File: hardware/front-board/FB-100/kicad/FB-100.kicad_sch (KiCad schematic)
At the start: 0 parts

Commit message: Close LB FB schematic freeze
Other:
- note added: "Reviewed FB-100 value-bearing schematic inputs: - JFB1 24-pin interface with USB_D_P, USB_D_N, USB_CC1, USB_CC2, USB_VBUS_SENSE, FB_3V3_IO, GND, status RGB, CH_LED_1..CH_LED_10, SERVICE_BTN, RESET_BTN, OLED_SCL, OLED_SDA. - USB-C service is device-only; CC Rd behavior; ESD protection; VBUS sense-only; no back-power into LB-100 or PB-100. - UI hardware stays role-free: channel/status indicators on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"
- note added: "Schematic freeze evidence: - ../FB-100-schematic-review-closeout.md - ../FB-100-interface-signal-plan.csv - ../FB-100-interface-pinout-closeout.csv - ../FB-100-usb-service-closeout-precheck.csv - ../FB-100-ui-control-closeout-precheck.csv - ../FB-100-ui-mechanical-precheck.csv - ../FB-100-mechanical-envelope-precheck.csv - ../FB-100-component-sourcing-precheck.csv PCB layout and manufacturing out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"
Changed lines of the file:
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@@
+    )
+  )
+  (text "Reviewed FB-100 value-bearing schematic inputs:\n- JFB1 24-pin interface with USB_D_P, USB_D_N, USB_CC1, USB_CC2, USB_VBUS_SENSE, FB_3V3_IO, GND, status RGB, CH_LED_1..CH_LED_10, SERVICE_BTN, RESET_BTN, OLED_SCL, OLED_SDA.\n- USB-C service is device-only; CC Rd behavior; ESD protection; VBUS sense-only; no back-power into LB-100 or PB-100.\n- UI hardware stays role-free: channel/status indicators only, no accessory names.\n- Optional OLED remains DNP until mechanical and power review.\n- Mechanical envelope, USB access, LED/button alignment, service sealing, and enclosure boundary are reviewed."
+    (at 130 30 0)
+    (effects
+      (font
+        (size 1.45 1.45)
+      )
+      (justify left top)
+    )
+  )
+  (text "Schematic freeze evidence:\n- ../FB-100-schematic-review-closeout.md\n- ../FB-100-interface-signal-plan.csv\n- ../FB-100-interface-pinout-closeout.csv\n- ../FB-100-usb-service-closeout-precheck.csv\n- ../FB-100-ui-control-closeout-precheck.csv\n- ../FB-100-ui-mechanical-precheck.csv\n- ../FB-100-mechanical-envelope-precheck.csv\n- ../FB-100-component-sourcing-precheck.csv\n\nPCB layout and manufacturing outputs remain separate post-freeze work."
+    (at 130 120 0)
+    (effects
+      (font
+        (size 1.45 1.45)
+      )
+      (justify left top)
     )
   )

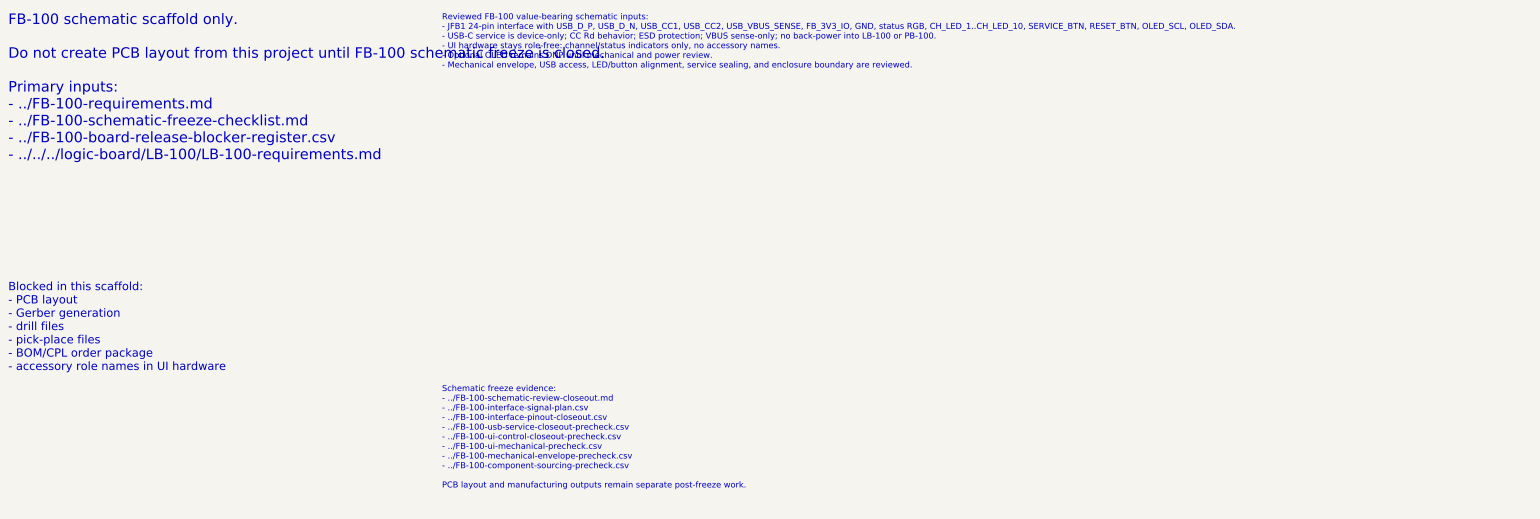
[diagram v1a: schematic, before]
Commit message: Add three-board footprint binding inventory
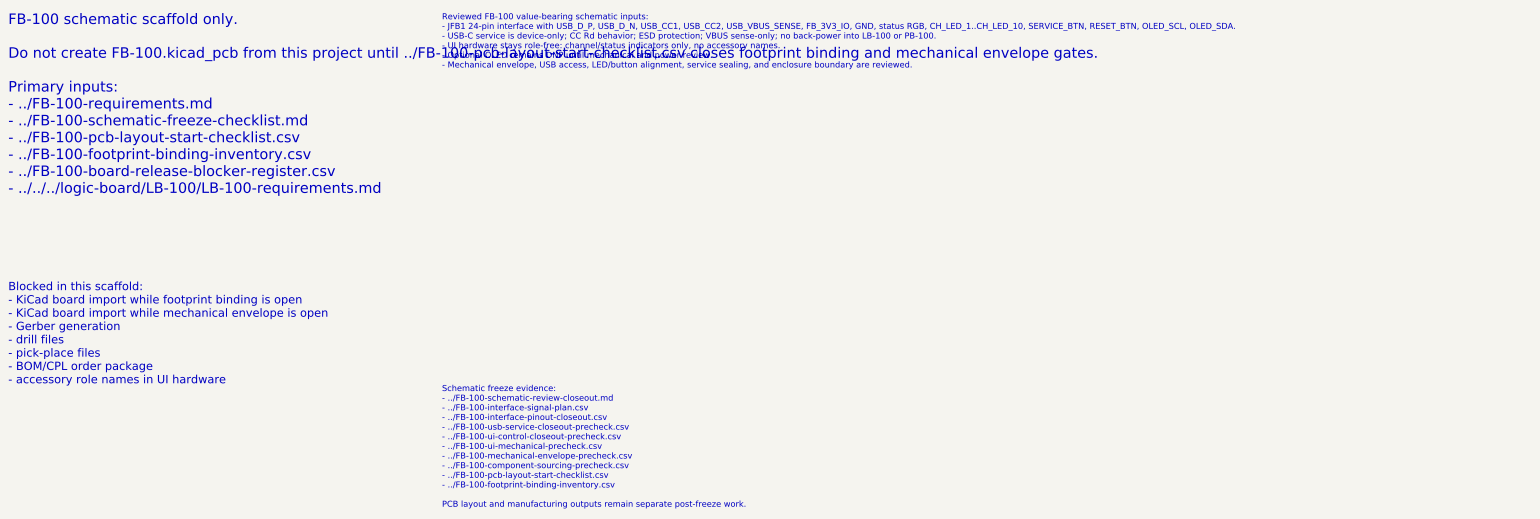
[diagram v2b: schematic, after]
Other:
- note added: "Blocked in this scaffold: - KiCad board import while footprint binding is open - KiCad board import while mechanical envelope is open - Gerber generation - drill files - pick-place files - BOM/CPL order package - accessory role names in UI hardware"
- note added: "FB-100 schematic scaffold only. Do not create FB-100.kicad_pcb from this project until ../FB-100-pcb-layout-start-checklist.csv closes footprint binding and mechanical envelope gates. Primary inputs: - ../FB-100-requirements.md - ../FB-100-schematic-freeze-checklist.md - ../FB-100-pcb-layout-start-checklist.csv - ../FB-100-footprint-binding-inventory.csv - ../FB-100-board-release-blocker-register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"
- note added: "Schematic freeze evidence: - ../FB-100-schematic-review-closeout.md - ../FB-100-interface-signal-plan.csv - ../FB-100-interface-pinout-closeout.csv - ../FB-100-usb-service-closeout-precheck.csv - ../FB-100-ui-control-closeout-precheck.csv - ../FB-100-ui-mechanical-precheck.csv - ../FB-100-mechanical-envelope-precheck.csv - ../FB-100-component-sourcing-precheck.csv - ../FB-100-pcb-layout-start-che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"
- note removed: "Blocked in this scaffold: - PCB layout - Gerber generation - drill files - pick-place files - BOM/CPL order package - accessory role names in UI hardware"
- note removed: "FB-100 schematic scaffold only. Do not create PCB layout from this project until FB-100 schematic freeze is closed. Primary inputs: - ../FB-100-requirements.md - ../FB-100-schematic-freeze-checklist.md - ../FB-100-board-release-blocker-register.csv - ../../../logic-board/LB-100/LB-100-requirements.md"
- note removed: "Schematic freeze evidence: - ../FB-100-schematic-review-closeout.md - ../FB-100-interface-signal-plan.csv - ../FB-100-interface-pinout-closeout.csv - ../FB-100-usb-service-closeout-precheck.csv - ../FB-100-ui-control-closeout-precheck.csv - ../FB-100-ui-mechanical-precheck.csv - ../FB-100-mechanical-envelope-precheck.csv - ../FB-100-component-sourcing-precheck.csv PCB layout and manufacturing out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"
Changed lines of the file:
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@@
     (rev "schematic-scaffold")
     (company "SVC Platform")
-    (comment 1 "Schematic scaffold only. PCB layout is blocked until FB-100 schematic freeze.")
+    (comment 1 "Schematic freeze closed. Board import is blocked by layout-start gates.")
     (comment 2 "Requirements: ../FB-100-requirements.md and ADR-0014.")
     (comment 3 "UI signals remain role-free status/channel signals.")
     (comment 4 "USB service path must not back-power LB-100 or PB-100 unless reviewed.")
   )
-  (text "FB-100 schematic scaffold only.\n\nDo not create PCB layout from this project until FB-100 schematic freeze is closed.\n\nPrimary inputs:\n- ../FB-100-requirements.md\n- ../FB-100-schematic-freeze-checklist.md\n- ../FB-100-board-release-blocker-register.csv\n- ../../../logic-board/LB-100/LB-100-requirements.md"
+  (text "FB-100 schematic scaffold only.\n\nDo not create FB-100.kicad_pcb from this project until ../FB-100-pcb-layout-start-checklist.csv closes footprint binding and mechanical envelope gates.\n\nPrimary inputs:\n- ../FB-100-requirements.md\n- ../FB-100-schematic-freeze-checklist.md\n- ../FB-100-pcb-layout-start-checklist.csv\n- ../FB-100-footprint-binding-inventory.csv\n- ../FB-100-board-release-blocker-register.csv\n- ../../../logic-board/LB-100/LB-100-requirements.md"
     (at 25 30 0)
     (effects
@@
     )
   )
-  (text "Blocked in this scaffold:\n- PCB layout\n- Gerber generation\n- drill files\n- pick-place files\n- BOM/CPL order package\n- accessory role names in UI hardware"
+  (text "Blocked in this scaffold:\n- KiCad board import while footprint binding is open\n- KiCad board import while mechanical envelope is open\n- Gerber generation\n- drill files\n- pick-place files\n- BOM/CPL order package\n- accessory role names in UI hardware"
     (at 25 95 0)
     (effects
@@
     )
   )
-  (text "Schematic freeze evidence:\n- ../FB-100-schematic-review-closeout.md\n- ../FB-100-interface-signal-plan.csv\n- ../FB-100-interface-pinout-closeout.csv\n- ../FB-100-usb-service-closeout-precheck.csv\n- ../FB-100-ui-control-closeout-precheck.csv\n- ../FB-100-ui-mechanical-precheck.csv\n- ../FB-100-mechanical-envelope-precheck.csv\n- ../FB-100-component-sourcing-precheck.csv\n\nPCB layout and manufacturing outputs remain separate post-freeze work."
+  (text "Schematic freeze evidence:\n- ../FB-100-schematic-review-closeout.md\n- ../FB-100-interface-signal-plan.csv\n- ../FB-100-interface-pinout-closeout.csv\n- ../FB-100-usb-service-closeout-precheck.csv\n- ../FB-100-ui-control-closeout-precheck.csv\n- ../FB-100-ui-mechanical-precheck.csv\n- ../FB-100-mechanical-envelope-precheck.csv\n- ../FB-100-component-sourcing-precheck.csv\n- ../FB-100-pcb-layout-start-checklist.csv\n- ../FB-100-footprint-binding-inventory.csv\n\nPCB layout and manufacturing outputs remain separate post-freeze work."
     (at 130 120 0)
     (effects
